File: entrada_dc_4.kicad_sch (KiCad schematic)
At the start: 4 parts

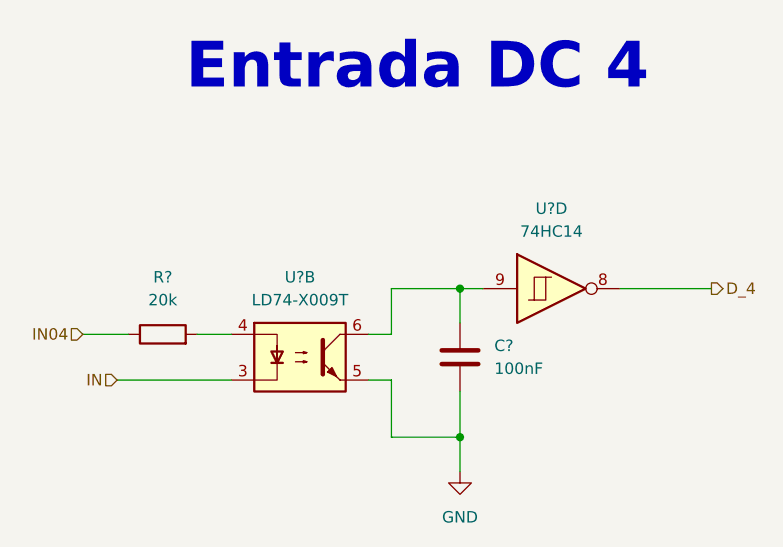
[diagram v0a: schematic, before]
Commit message: input/output separadas
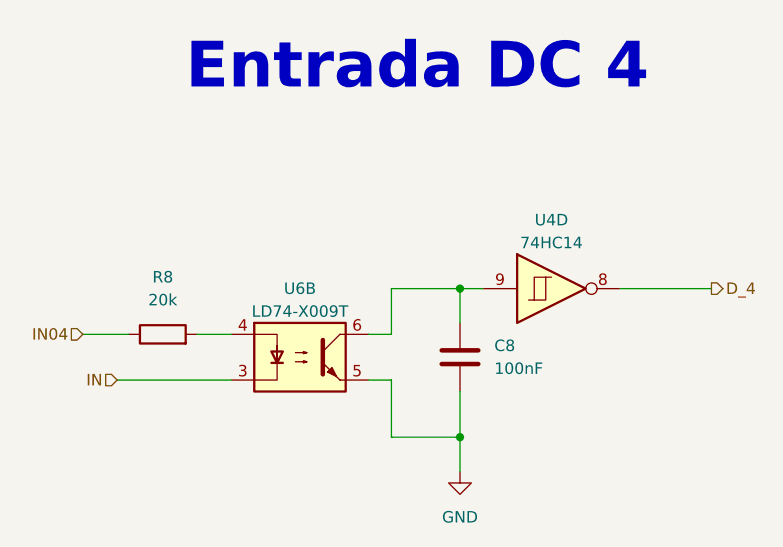
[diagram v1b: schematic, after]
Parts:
- gave numbers to parts that had none: 4
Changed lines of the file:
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@@
 (kicad_sch (version 20221004) (generator eeschema)
   (paper "A4" portrait)
+  (title_block
+    (date "2022-10-09")
+    (rev "José Luis Laica")
+  )
   (junction (at 120.65 114.3) (diameter 0) (color 0 0 0 0)
   )
@@
   (symbol (lib_id "Device:C") (at 120.65 121.92 0) (unit 1)
     (in_bom yes) (on_board yes) (dnp no) (fields_autoplaced)
-    (property "Reference" "C?" (at 124.46 120.6499 0)
+    (property "Reference" "C8" (at 124.46 120.6499 0)
       (effects (font (size 1.27 1.27)) (justify left))
     )
@@
       (project "PLC 32 V2"
         (path "/d17a54f1-6eda-453f-95e1-42a53b02a1c3/c71b7323-b7b3-4df1-8a4f-adfbd95d7a33"
-          (reference "C?") (unit 1) (value "100nF") (footprint "Capacitor_SMD:C_0402_1005Metric")
+          (reference "C8") (unit 1) (value "100nF") (footprint "Capacitor_SMD:C_0402_1005Metric")
         )
       )
@@
   (symbol (lib_id "74xx:74HC14") (at 130.81 114.3 0) (unit 4)
     (in_bom yes) (on_board yes) (dnp no) (fields_autoplaced)
-    (property "Reference" "U?" (at 130.81 105.41 0)
+    (property "Reference" "U4" (at 130.81 106.68 0)
       (effects (font (size 1.27 1.27)))
     )
-    (property "Value" "74HC14" (at 130.81 107.95 0)
+    (property "Value" "74HC14" (at 130.81 109.22 0)
       (effects (font (size 1.27 1.27)))
     )
@@
       (project "PLC 32 V2"
         (path "/d17a54f1-6eda-453f-95e1-42a53b02a1c3/c71b7323-b7b3-4df1-8a4f-adfbd95d7a33"
-          (reference "U?") (unit 4) (value "74HC14") (footprint "Package_SO:SOIC-14W_7.5x9mm_P1.27mm")
+          (reference "U4") (unit 4) (value "74HC14") (footprint "Package_SO:SOIC-14W_7.5x9mm_P1.27mm")
         )
       )
@@
   (symbol (lib_id "power:GND") (at 120.65 134.62 0) (unit 1)
     (in_bom yes) (on_board yes) (dnp no) (fields_autoplaced)
-    (property "Reference" "#PWR?" (at 120.65 140.97 0)
+    (property "Reference" "#PWR09" (at 120.65 140.97 0)
       (effects (font (size 1.27 1.27)) hide)
     )
@@
       (project "PLC 32 V2"
         (path "/d17a54f1-6eda-453f-95e1-42a53b02a1c3/c71b7323-b7b3-4df1-8a4f-adfbd95d7a33"
-          (reference "#PWR?") (unit 1) (value "GND") (footprint "")
+          (reference "#PWR09") (unit 1) (value "GND") (footprint "")
         )
       )
@@
   (symbol (lib_id "Device:R") (at 87.63 119.38 90) (unit 1)
     (in_bom yes) (on_board yes) (dnp no) (fields_autoplaced)
-    (property "Reference" "R?" (at 87.63 113.03 90)
+    (property "Reference" "R8" (at 87.63 113.03 90)
       (effects (font (size 1.27 1.27)))
     )
@@
       (project "PLC 32 V2"
         (path "/d17a54f1-6eda-453f-95e1-42a53b02a1c3/c71b7323-b7b3-4df1-8a4f-adfbd95d7a33"
-          (reference "R?") (unit 1) (value "20k") (footprint "Resistor_SMD:R_0603_1608Metric")
+          (reference "R8") (unit 1) (value "20k") (footprint "Resistor_SMD:R_0603_1608Metric")
         )
       )
@@
   (symbol (lib_id "Isolator:ILD74") (at 102.87 121.92 0) (unit 2)
     (in_bom yes) (on_board yes) (dnp no) (fields_autoplaced)
-    (property "Reference" "U?" (at 102.87 113.03 0)
+    (property "Reference" "U6" (at 102.87 114.3 0)
       (effects (font (size 1.27 1.27)))
     )
-    (property "Value" "LD74-X009T" (at 102.87 115.57 0)
+    (property "Value" "LD74-X009T" (at 102.87 116.84 0)
       (effects (font (size 1.27 1.27)))
     )
@@
       (project "PLC 32 V2"
         (path "/d17a54f1-6eda-453f-95e1-42a53b02a1c3/c71b7323-b7b3-4df1-8a4f-adfbd95d7a33"
-          (reference "U?") (unit 2) (value "LD74-X009T") (footprint "Package_DIP:DIP-8_W8.89mm_SMDSocket_LongPads")
+          (reference "U6") (unit 2) (value "LD74-X009T") (footprint "Package_DIP:DIP-8_W8.89mm_SMDSocket_LongPads")
         )
       )

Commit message: add
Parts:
- renumbered C8 to C9, R8 to R38, U4 to U7, U6 to U9
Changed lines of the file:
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@@
   (symbol (lib_id "Device:C") (at 120.65 121.92 0) (unit 1)
     (in_bom yes) (on_board yes) (dnp no) (fields_autoplaced)
-    (property "Reference" "C8" (at 124.46 120.6499 0)
+    (property "Reference" "C9" (at 124.46 120.6499 0)
       (effects (font (size 1.27 1.27)) (justify left))
     )
@@
       (project "PLC 32 V2"
         (path "/d17a54f1-6eda-453f-95e1-42a53b02a1c3/c71b7323-b7b3-4df1-8a4f-adfbd95d7a33"
-          (reference "C8") (unit 1) (value "100nF") (footprint "Capacitor_SMD:C_0402_1005Metric")
+          (reference "C9") (unit 1) (value "100nF") (footprint "Capacitor_SMD:C_0402_1005Metric")
         )
       )
@@
   (symbol (lib_id "74xx:74HC14") (at 130.81 114.3 0) (unit 4)
     (in_bom yes) (on_board yes) (dnp no) (fields_autoplaced)
-    (property "Reference" "U4" (at 130.81 106.68 0)
+    (property "Reference" "U7" (at 130.81 106.68 0)
       (effects (font (size 1.27 1.27)))
     )
@@
       (project "PLC 32 V2"
         (path "/d17a54f1-6eda-453f-95e1-42a53b02a1c3/c71b7323-b7b3-4df1-8a4f-adfbd95d7a33"
-          (reference "U4") (unit 4) (value "74HC14") (footprint "Package_SO:SOIC-14W_7.5x9mm_P1.27mm")
+          (reference "U7") (unit 4) (value "74HC14") (footprint "Package_SO:SOIC-14W_7.5x9mm_P1.27mm")
         )
       )
@@
   (symbol (lib_id "Device:R") (at 87.63 119.38 90) (unit 1)
     (in_bom yes) (on_board yes) (dnp no) (fields_autoplaced)
-    (property "Reference" "R8" (at 87.63 113.03 90)
+    (property "Reference" "R38" (at 87.63 113.03 90)
       (effects (font (size 1.27 1.27)))
     )
@@
       (project "PLC 32 V2"
         (path "/d17a54f1-6eda-453f-95e1-42a53b02a1c3/c71b7323-b7b3-4df1-8a4f-adfbd95d7a33"
-          (reference "R8") (unit 1) (value "20k") (footprint "Resistor_SMD:R_0603_1608Metric")
+          (reference "R38") (unit 1) (value "20k") (footprint "Resistor_SMD:R_0603_1608Metric")
         )
       )
@@
   (symbol (lib_id "Isolator:ILD74") (at 102.87 121.92 0) (unit 2)
     (in_bom yes) (on_board yes) (dnp no) (fields_autoplaced)
-    (property "Reference" "U6" (at 102.87 114.3 0)
+    (property "Reference" "U9" (at 102.87 114.3 0)
       (effects (font (size 1.27 1.27)))
     )
@@
       (project "PLC 32 V2"
         (path "/d17a54f1-6eda-453f-95e1-42a53b02a1c3/c71b7323-b7b3-4df1-8a4f-adfbd95d7a33"
-          (reference "U6") (unit 2) (value "LD74-X009T") (footprint "Package_DIP:DIP-8_W8.89mm_SMDSocket_LongPads")
+          (reference "U9") (unit 2) (value "LD74-X009T") (footprint "Package_DIP:DIP-8_W8.89mm_SMDSocket_LongPads")
         )
       )
